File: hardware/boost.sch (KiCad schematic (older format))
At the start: 10 parts, among them SW1 SW_SPST, U2 TPS61022

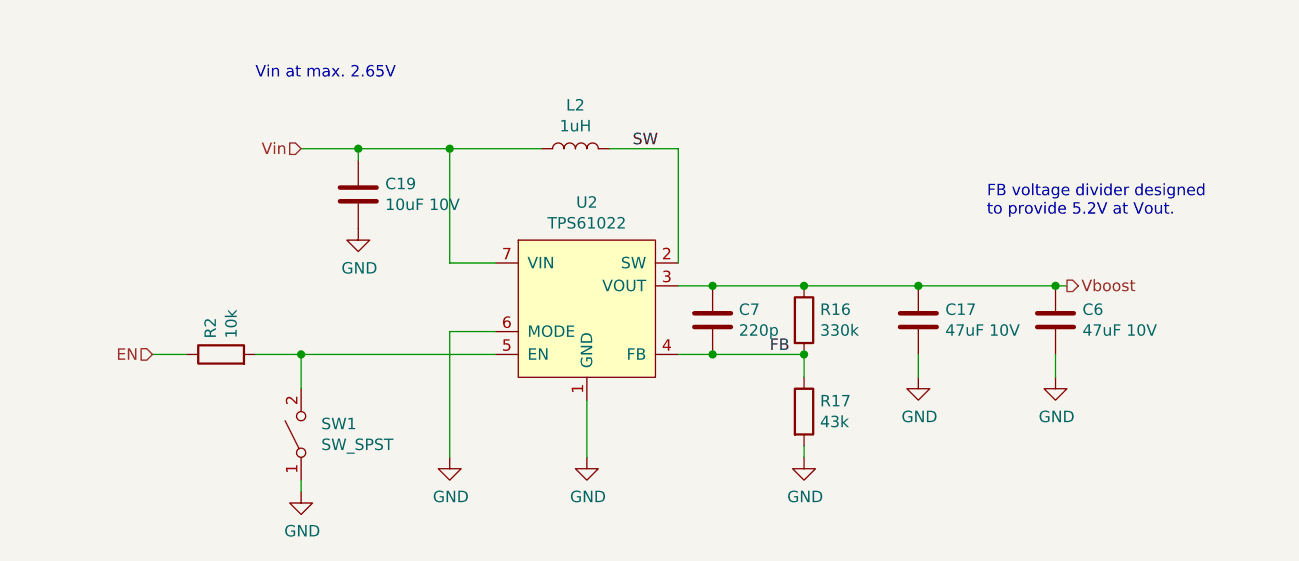
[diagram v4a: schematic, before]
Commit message: Redesign SMPS layouts.
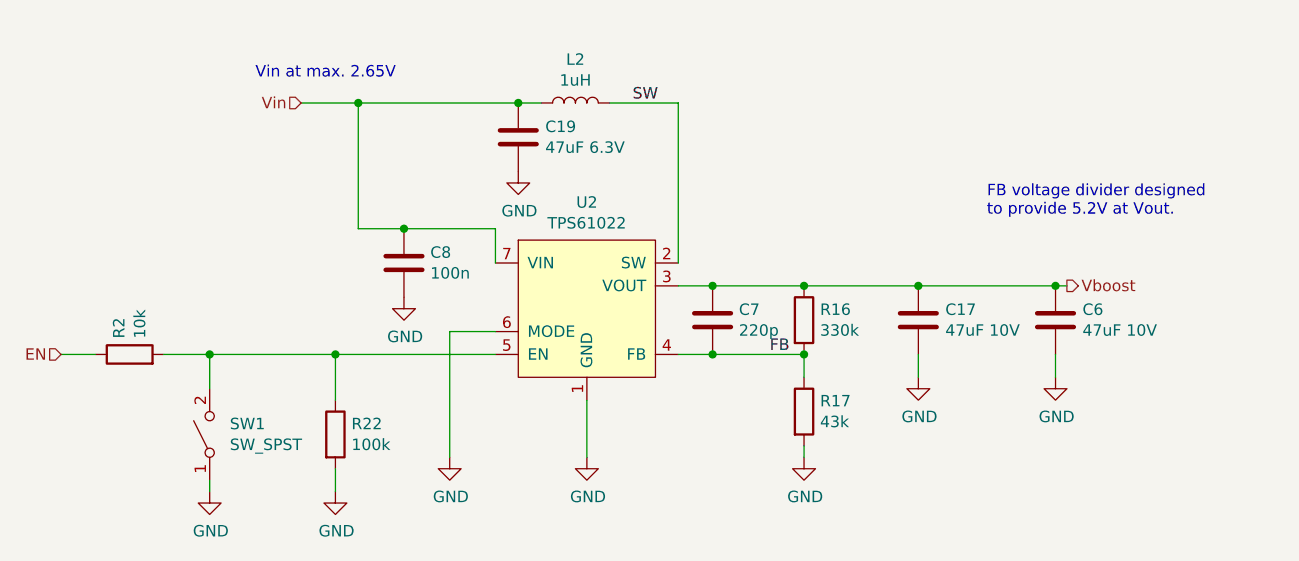
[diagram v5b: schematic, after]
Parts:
- added C8: 100n, Capacitor_SMD:C_0603_1608Metric_Pad1.05x0.95mm_HandSolder, symbol Device:C
- added R22: 100k, Resistor_SMD:R_0603_1608Metric_Pad1.05x0.95mm_HandSolder, symbol Device:R
- C17, C6: footprint Capacitor_SMD:C_1206_3216Metric_Pad1.42x1.75mm_HandSolder -> Capacitor_SMD:C_0805_2012Metric_Pad1.15x1.40mm_HandSolder
- C19: value 10uF 10V -> 47uF 6.3V; footprint Capacitor_SMD:C_0603_1608Metric_Pad1.05x0.95mm_HandSolder -> Capacitor_SMD:C_0805_2012Metric_Pad1.15x1.40mm_HandSolder
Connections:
- net GND: now also C8.2, R22.2
- net Vin: now also C8.1
- net at R2.2, SW1.2 (B), U2.5 (EN): now also R22.1
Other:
- moved on the sheet: C19, L2, R2, SW1
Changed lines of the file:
@@
 F 0 "C17" H 4968 2496 50  0000 L CNN
 F 1 "47uF 10V" H 4968 2405 50  0000 L CNN
-F 2 "Capacitor_SMD:C_1206_3216Metric_Pad1.42x1.75mm_HandSolder" H 4888 2300 50  0001 C CNN
+F 2 "Capacitor_SMD:C_0805_2012Metric_Pad1.15x1.40mm_HandSolder" H 4888 2300 50  0001 C CNN
 F 3 "~" H 4850 2450 50  0001 C CNN
 	1    4850 2450
@@
 L Device:L L?
 U 1 1 5CA6B4FC
-P 3350 1700
+P 3350 1500
 AR Path="/5C3480BB/5CA6B4FC" Ref="L?"  Part="1"
 AR Path="/5CA73F16/5CA6B4FC" Ref="L2"  Part="1"
-F 0 "L2" V 3540 1700 50  0000 C CNN
-F 1 "1uH" V 3449 1700 50  0000 C CNN
-F 2 "Inductor_SMD:L_Abracon_ASPI-0630LR" H 3350 1700 50  0001 C CNN
-F 3 "" H 3350 1700 50  0001 C CNN
-F 4 "Shun Xiang Nuo Elec SMMS0630-1R0M" V 3350 1700 50  0001 C CNN "Notes"
-	1    3350 1700
+F 0 "L2" V 3540 1500 50  0000 C CNN
+F 1 "1uH" V 3449 1500 50  0000 C CNN
+F 2 "Inductor_SMD:L_Abracon_ASPI-0630LR" H 3350 1500 50  0001 C CNN
+F 3 "" H 3350 1500 50  0001 C CNN
+F 4 "Shun Xiang Nuo Elec SMMS0630-1R0M" V 3350 1500 50  0001 C CNN "Notes"
+	1    3350 1500
 	0    -1   -1   0
 $EndComp
 Wire Wire Line
-	3000 2200 2800 2200
-Wire Wire Line
-	2800 2200 2800 1700
-Connection ~ 2800 1700
-Wire Wire Line
-	2800 1700 3200 1700
-Wire Wire Line
-	3800 2200 3800 1700
-Wire Wire Line
-	3800 1700 3500 1700
+	3000 2050 2600 2050
+Wire Wire Line
+	2400 1500 3100 1500
+Wire Wire Line
+	3800 1500 3500 1500
 $Comp
 L Device:R R?
@@
 	4850 2700 4850 2600
 Wire Wire Line
-	2150 1700 2400 1700
-Text Label 3600 1700 0    50   ~ 0
+	2150 1500 2400 1500
+Text Label 3600 1500 0    50   ~ 0
 SW
 Text Label 4200 2600 0    50   ~ 0
 FB
-Text HLabel 2150 1700 0    50   Input ~ 0
+Text HLabel 2150 1500 0    50   Input ~ 0
 Vin
 Wire Wire Line
@@
 L Device:C C?
 U 1 1 5CF608F8
-P 2400 1900
+P 3100 1650
 AR Path="/5CF608F8" Ref="C?"  Part="1"
 AR Path="/5C3480BB/5CF608F8" Ref="C?"  Part="1"
 AR Path="/5CA73F16/5CF608F8" Ref="C19"  Part="1"
-F 0 "C19" H 2518 1946 50  0000 L CNN
-F 1 "10uF 10V" H 2518 1855 50  0000 L CNN
-F 2 "Capacitor_SMD:C_0603_1608Metric_Pad1.05x0.95mm_HandSolder" H 2438 1750 50  0001 C CNN
-F 3 "~" H 2400 1900 50  0001 C CNN
-	1    2400 1900
-	1    0    0    -1
-$EndComp
-Wire Wire Line
-	2400 1750 2400 1700
-Connection ~ 2400 1700
-Wire Wire Line
-	2400 1700 2800 1700
+F 0 "C19" H 3218 1696 50  0000 L CNN
+F 1 "47uF 6.3V" H 3218 1605 50  0000 L CNN
+F 2 "Capacitor_SMD:C_0805_2012Metric_Pad1.15x1.40mm_HandSolder" H 3138 1500 50  0001 C CNN
+F 3 "~" H 3100 1650 50  0001 C CNN
+	1    3100 1650
+	1    0    0    -1
+$EndComp
 $Comp
 L power:GND #PWR?
 U 1 1 5CF60DAB
-P 2400 2050
+P 3100 1800
 AR Path="/5CF60DAB" Ref="#PWR?"  Part="1"
 AR Path="/5C3480BB/5CF60DAB" Ref="#PWR?"  Part="1"
 AR Path="/5CA73F16/5CF60DAB" Ref="#PWR0104"  Part="1"
-F 0 "#PWR0104" H 2400 1800 50  0001 C CNN
-F 1 "GND" H 2405 1877 50  0000 C CNN
-F 2 "" H 2400 2050 50  0001 C CNN
-F 3 "" H 2400 2050 50  0001 C CNN
-	1    2400 2050
-	1    0    0    -1
-$EndComp
-Text HLabel 1500 2600 0    50   Input ~ 0
+F 0 "#PWR0104" H 3100 1550 50  0001 C CNN
+F 1 "GND" H 3105 1627 50  0000 C CNN
+F 2 "" H 3100 1800 50  0001 C CNN
+F 3 "" H 3100 1800 50  0001 C CNN
+	1    3100 1800
+	1    0    0    -1
+$EndComp
+Text HLabel 1100 2600 0    50   Input ~ 0
 EN
 $Comp
@@
 $EndComp
 Wire Wire Line
-	1500 2600 1650 2600
+	1100 2600 1250 2600
 $Comp
 L power:GND #PWR?
@@
 L Switch:SW_SPST SW1
 U 1 1 5D5B325B
-P 2150 2950
-F 0 "SW1" V 2196 2862 50  0000 R CNN
-F 1 "SW_SPST" V 2105 2862 50  0000 R CNN
-F 2 "Connector_PinHeader_2.54mm:PinHeader_1x02_P2.54mm_Vertical" H 2150 2950 50  0001 C CNN
-F 3 "~" H 2150 2950 50  0001 C CNN
-	1    2150 2950
+P 1750 2950
+F 0 "SW1" V 1796 2862 50  0000 R CNN
+F 1 "SW_SPST" V 1705 2862 50  0000 R CNN
+F 2 "Connector_PinHeader_2.54mm:PinHeader_1x02_P2.54mm_Vertical" H 1750 2950 50  0001 C CNN
+F 3 "~" H 1750 2950 50  0001 C CNN
+	1    1750 2950
 	0    -1   -1   0
 $EndComp
@@
 L Device:R R?
 U 1 1 5D5B16A2
-P 1800 2600
+P 1400 2600
 AR Path="/5D5B16A2" Ref="R?"  Part="1"
 AR Path="/5C3480BB/5D5B16A2" Ref="R?"  Part="1"
 AR Path="/5CA73F16/5D5B16A2" Ref="R2"  Part="1"
-F 0 "R2" H 1870 2646 50  0000 L CNN
-F 1 "10k" H 1870 2555 50  0000 L CNN
-F 2 "Resistor_SMD:R_0603_1608Metric_Pad1.05x0.95mm_HandSolder" V 1730 2600 50  0001 C CNN
-F 3 "~" H 1800 2600 50  0001 C CNN
-	1    1800 2600
+F 0 "R2" H 1470 2646 50  0000 L CNN
+F 1 "10k" H 1470 2555 50  0000 L CNN
+F 2 "Resistor_SMD:R_0603_1608Metric_Pad1.05x0.95mm_HandSolder" V 1330 2600 50  0001 C CNN
+F 3 "~" H 1400 2600 50  0001 C CNN
+	1    1400 2600
 	0    -1   -1   0
 $EndComp
 Wire Wire Line
-	1950 2600 2150 2600
-Wire Wire Line
-	2150 2750 2150 2600
-Connection ~ 2150 2600
-Wire Wire Line
-	2150 2600 3000 2600
+	1550 2600 1750 2600
+Wire Wire Line
+	1750 2750 1750 2600
+Connection ~ 1750 2600
 $Comp
 L power:GND #PWR?
 U 1 1 5D5B5E50
-P 2150 3200
+P 1750 3200
 AR Path="/5D5B5E50" Ref="#PWR?"  Part="1"
 AR Path="/5C3480BB/5D5B5E50" Ref="#PWR?"  Part="1"
 AR Path="/5CA73F16/5D5B5E50" Ref="#PWR0108"  Part="1"
-F 0 "#PWR0108" H 2150 2950 50  0001 C CNN
-F 1 "GND" H 2155 3027 50  0000 C CNN
-F 2 "" H 2150 3200 50  0001 C CNN
-F 3 "" H 2150 3200 50  0001 C CNN
-	1    2150 3200
-	1    0    0    -1
-$EndComp
-Wire Wire Line
-	2150 3200 2150 3150
+F 0 "#PWR0108" H 1750 2950 50  0001 C CNN
+F 1 "GND" H 1755 3027 50  0000 C CNN
+F 2 "" H 1750 3200 50  0001 C CNN
+F 3 "" H 1750 3200 50  0001 C CNN
+	1    1750 3200
+	1    0    0    -1
+$EndComp
+Wire Wire Line
+	1750 3200 1750 3150
 $Comp
 L Device:C C?
@@
 F 0 "C6" H 5568 2496 50  0000 L CNN
 F 1 "47uF 10V" H 5568 2405 50  0000 L CNN
-F 2 "Capacitor_SMD:C_1206_3216Metric_Pad1.42x1.75mm_HandSolder" H 5488 2300 50  0001 C CNN
+F 2 "Capacitor_SMD:C_0805_2012Metric_Pad1.15x1.40mm_HandSolder" H 5488 2300 50  0001 C CNN
 F 3 "~" H 5450 2450 50  0001 C CNN
 	1    5450 2450
@@
 	1    0    0    -1
 $EndComp
+Wire Wire Line
+	1750 2600 2300 2600
+$Comp
+L Device:R R?
+U 1 1 5D91DD8E
+P 2300 2950
+AR Path="/5D91DD8E" Ref="R?"  Part="1"
+AR Path="/5C3480BB/5D91DD8E" Ref="R?"  Part="1"
+AR Path="/5CA73F16/5D91DD8E" Ref="R22"  Part="1"
+F 0 "R22" H 2370 2996 50  0000 L CNN
+F 1 "100k" H 2370 2905 50  0000 L CNN
+F 2 "Resistor_SMD:R_0603_1608Metric_Pad1.05x0.95mm_HandSolder" V 2230 2950 50  0001 C CNN
+F 3 "~" H 2300 2950 50  0001 C CNN
+	1    2300 2950
+	1    0    0    -1
+$EndComp
+Wire Wire Line
+	2300 2800 2300 2600
+Connection ~ 2300 2600
+Wire Wire Line
+	2300 2600 3000 2600
+Wire Wire Line
+	2300 3100 2300 3200
+$Comp
+L power:GND #PWR?
+U 1 1 5D91E379
+P 2300 3200
+AR Path="/5D91E379" Ref="#PWR?"  Part="1"
+AR Path="/5C3480BB/5D91E379" Ref="#PWR?"  Part="1"
+AR Path="/5CA73F16/5D91E379" Ref="#PWR025"  Part="1"
+F 0 "#PWR025" H 2300 2950 50  0001 C CNN
+F 1 "GND" H 2305 3027 50  0000 C CNN
+F 2 "" H 2300 3200 50  0001 C CNN
+F 3 "" H 2300 3200 50  0001 C CNN
+	1    2300 3200
+	1    0    0    -1
+$EndComp
+Wire Wire Line
+	3800 1500 3800 2200
+Connection ~ 3100 1500
+Wire Wire Line
+	3100 1500 3200 1500
+Wire Wire Line
+	2400 1500 2400 2050
+Connection ~ 2400 1500
+$Comp
+L Device:C C8
+U 1 1 5D9259A2
+P 2600 2200
+F 0 "C8" H 2715 2246 50  0000 L CNN
+F 1 "100n" H 2715 2155 50  0000 L CNN
+F 2 "Capacitor_SMD:C_0603_1608Metric_Pad1.05x0.95mm_HandSolder" H 2638 2050 50  0001 C CNN
+F 3 "~" H 2600 2200 50  0001 C CNN
+	1    2600 2200
+	1    0    0    -1
+$EndComp
+Wire Wire Line
+	3000 2050 3000 2200
+Connection ~ 2600 2050
+Wire Wire Line
+	2600 2050 2400 2050
+$Comp
+L power:GND #PWR?
+U 1 1 5D9260DB
+P 2600 2350
+AR Path="/5D9260DB" Ref="#PWR?"  Part="1"
+AR Path="/5C3480BB/5D9260DB" Ref="#PWR?"  Part="1"
+AR Path="/5CA73F16/5D9260DB" Ref="#PWR049"  Part="1"
+F 0 "#PWR049" H 2600 2100 50  0001 C CNN
+F 1 "GND" H 2605 2177 50  0000 C CNN
+F 2 "" H 2600 2350 50  0001 C CNN
+F 3 "" H 2600 2350 50  0001 C CNN
+	1    2600 2350
+	1    0    0    -1
+$EndComp
